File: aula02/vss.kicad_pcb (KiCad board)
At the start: 2 copper layers, 58 x 65 mm, 28 parts, among them J1 BATTERY, P1 MOTOR_L, P2 MOTOR_R, SW1 SW_SPST, U1 NUCLEO-F303K8, U2 SN754410, U3 LM78L05, U4 nRF24L01+

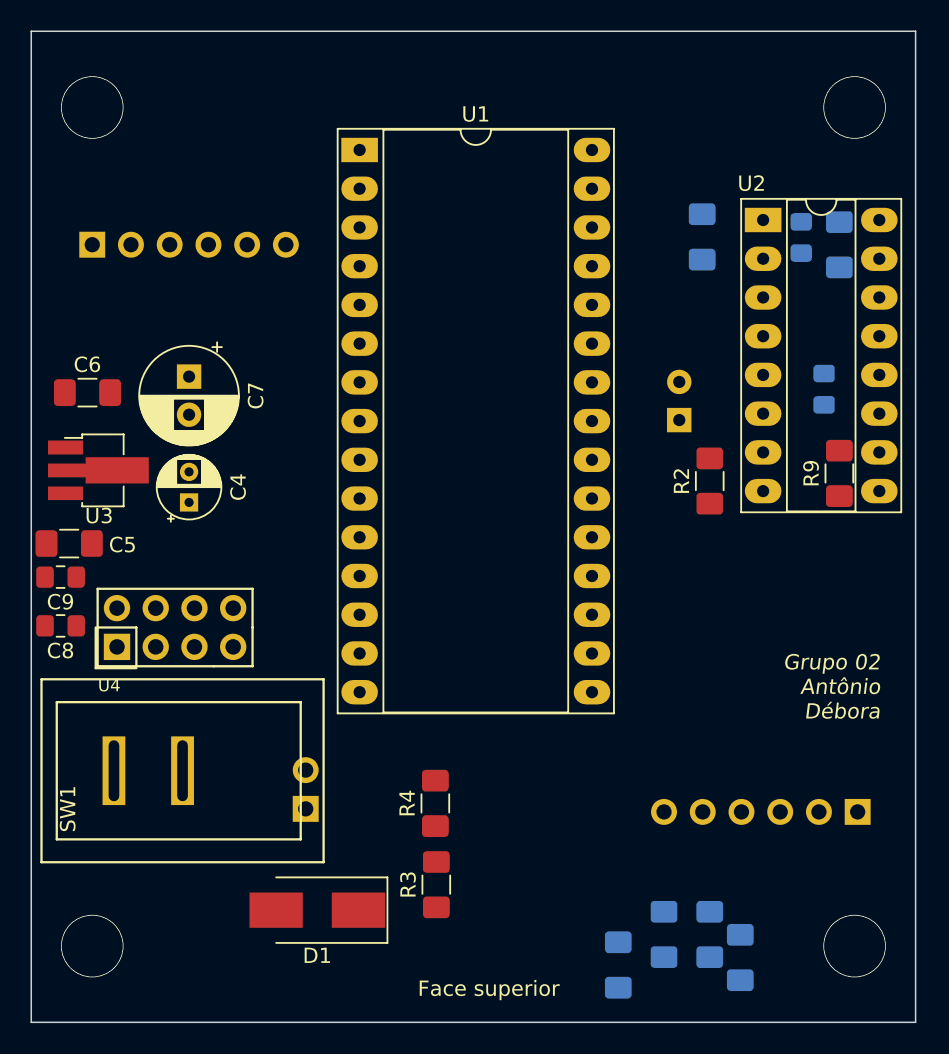
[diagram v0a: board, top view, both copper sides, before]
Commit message: feat: pcb roteamento
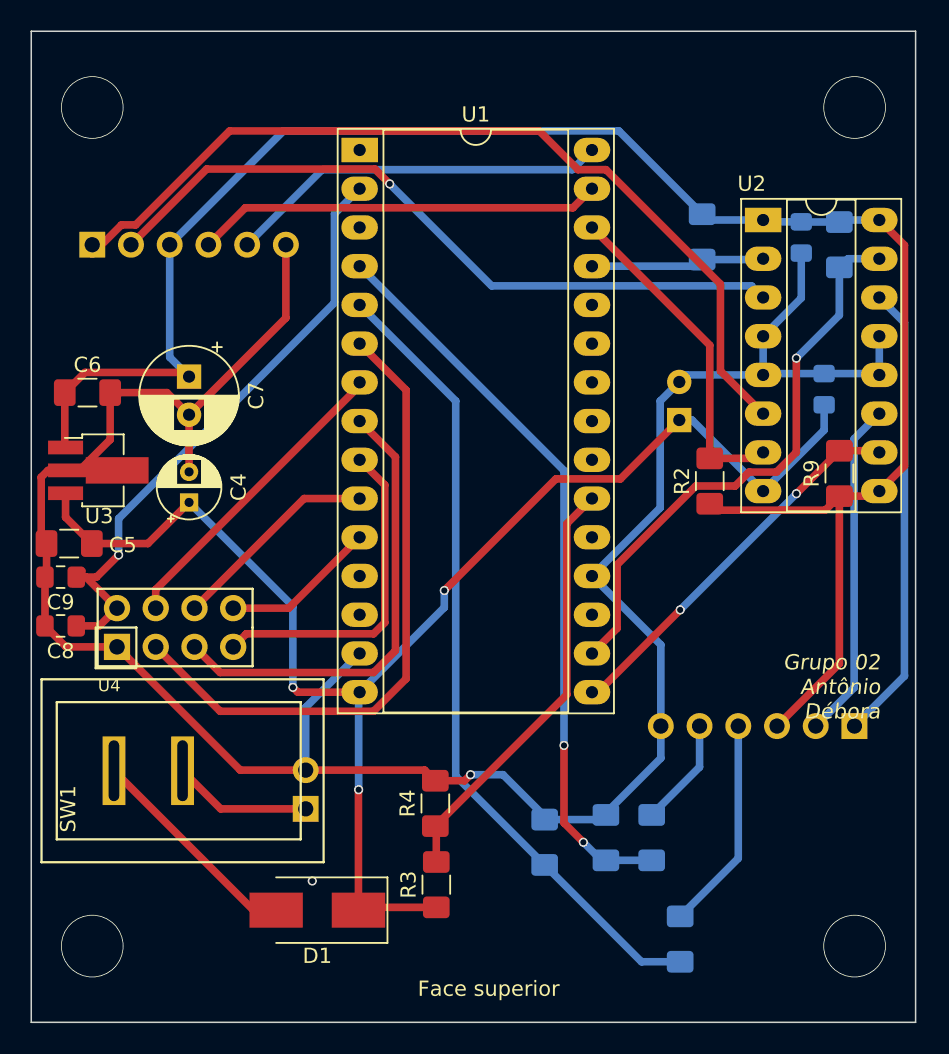
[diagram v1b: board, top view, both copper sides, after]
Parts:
- moved R7 9.39 mm to (153.7, 123.2)
- moved R6 7.41 mm to (160.7, 122.9)
- moved R8 7.41 mm to (157.7, 122.9)
- moved P2 5.63 mm to (174.0, 115.6)
- moved R5 4.12 mm to (162.6, 129.5)
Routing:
- net GND: track 0.00 -> 153.4 mm, vias 0 -> 1
- net +5V: track 0.00 -> 121.5 mm
- net +BATT: track 0.00 -> 95.4 mm, vias 0 -> 3
- net Net-(P1-Pad1): track 0.00 -> 59.0 mm
- net /MotorR/ENCODER_1: track 0.00 -> 53.3 mm
- net /MotorR/ENCODER_2: track 0.00 -> 48.8 mm, vias 0 -> 2
- net Net-(P1-Pad2): track 0.00 -> 47.0 mm, vias 0 -> 1
- net /Radio/CE: track 0.00 -> 42.3 mm
- net +3V3: track 0.00 -> 41.2 mm, vias 0 -> 1
- net /MotorR/PWM_2: track 0.00 -> 37.5 mm, vias 0 -> 1
- net /Radio/SCK: track 0.00 -> 30.5 mm
- net Net-(P2-Pad1): track 0.00 -> 30.2 mm
- net /Microcontroller/BATTERY_VOLTAGE: track 0.00 -> 28.1 mm
- net /MotorL/ENCODER_1: track 0.00 -> 26.7 mm
- net /MotorR/PWM_1: track 0.00 -> 25.8 mm, vias 0 -> 2
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
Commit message: fix: roteamento motor
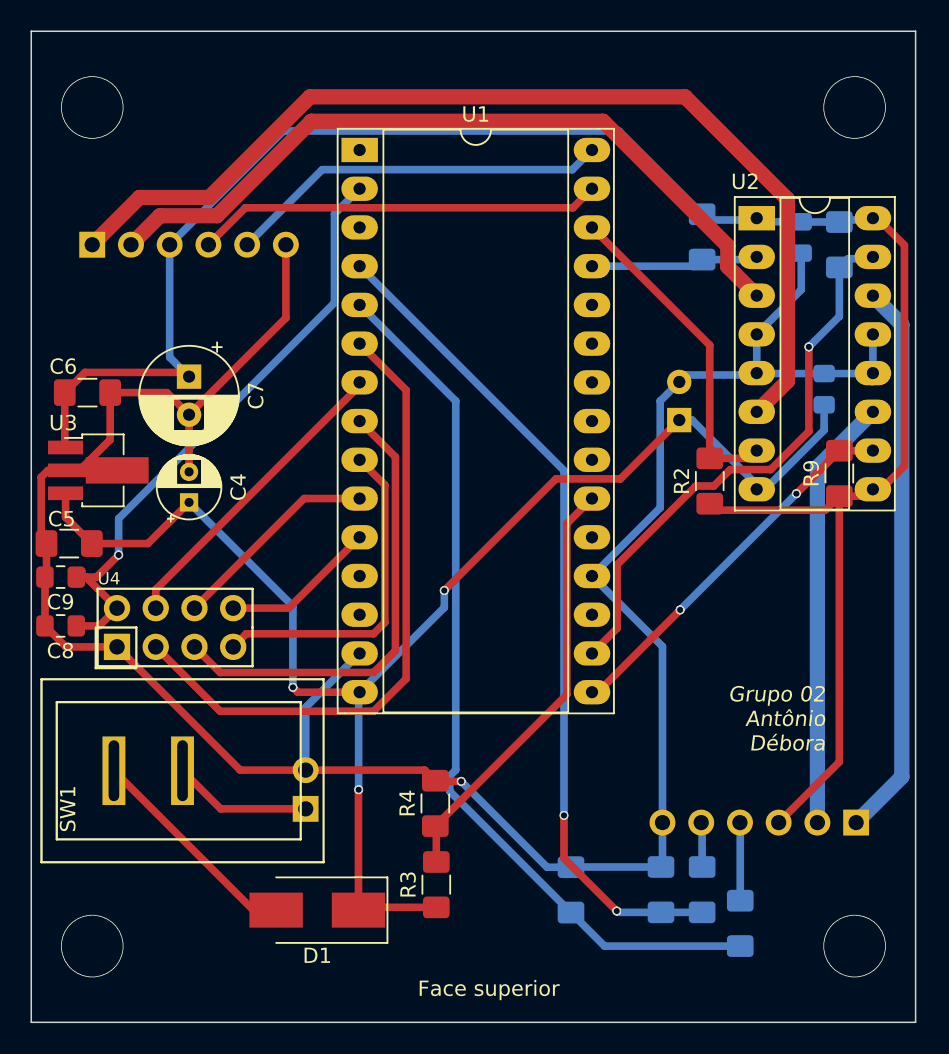
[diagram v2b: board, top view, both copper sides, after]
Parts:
- moved P2 6.33 mm to (174.1, 121.9)
- moved R8 4.97 mm to (161.3, 126.3)
- moved R6 4.75 mm to (164.0, 126.3)
- moved R5 4.07 mm to (166.5, 128.5)
- moved R7 3.57 mm to (155.4, 126.3)
- moved U2 0.44 mm to (167.6, 82.3)
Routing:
- net /MotorR/ENC_R_1: track 14.1 -> 5.13 mm
- net Net-(P1-Pad1): track 59.0 -> 67.8 mm
- net GND: track 153.4 -> 160.1 mm
- net Net-(P2-Pad1): track 30.2 -> 36.6 mm
- net +5V: track 121.5 -> 127.8 mm
- net Net-(P2-Pad2): track 22.2 -> 28.4 mm
- net /MotorR/ENCODER_2: track 48.8 -> 54.9 mm
- net /MotorR/ENCODER_1: track 53.3 -> 58.5 mm
- net /MotorR/ENC_R_2: track 7.13 -> 2.94 mm
- net Net-(P1-Pad2): track 47.0 -> 50.2 mm, vias 1 -> 0
- net (no net): vias 5 -> 4
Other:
- board text added: "GND"

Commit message: fix: roteamento motor
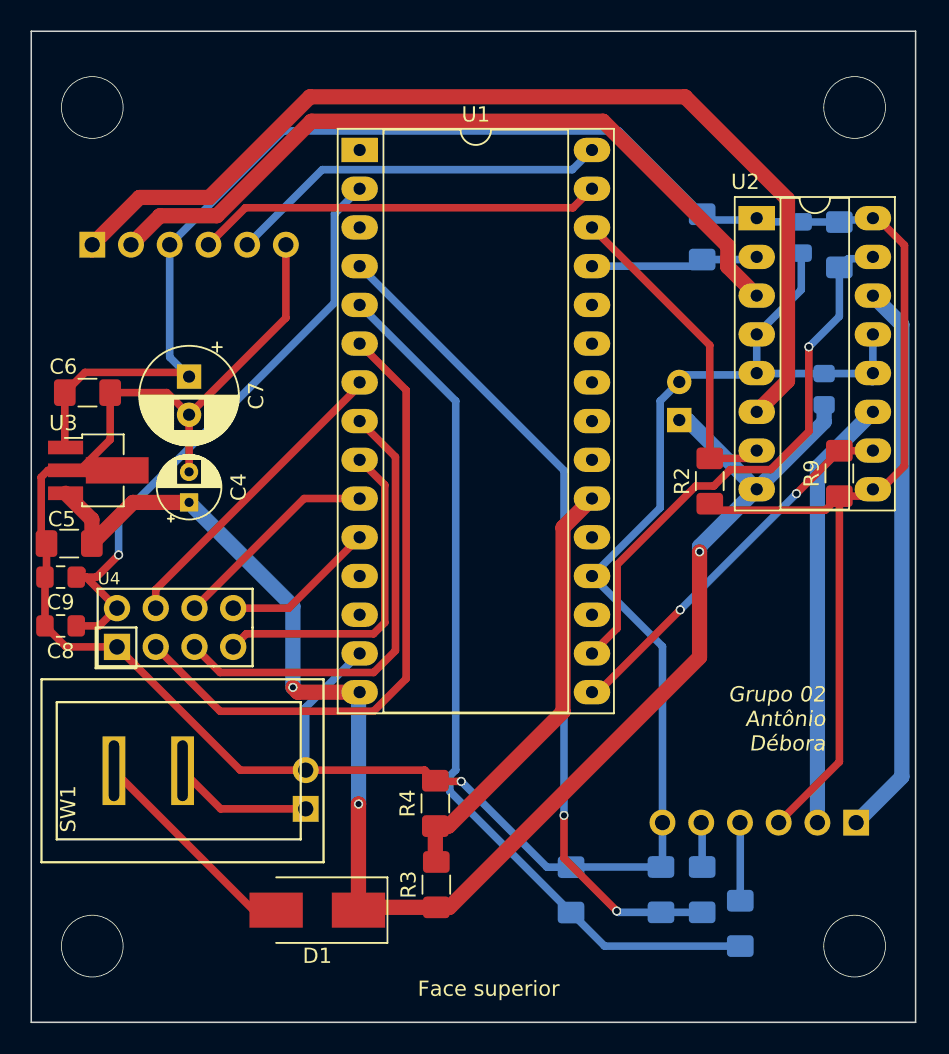
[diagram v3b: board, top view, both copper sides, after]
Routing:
- net +BATT: track 95.4 -> 102.8 mm
- net /Microcontroller/BATTERY_VOLTAGE: track 28.1 -> 28.7 mm

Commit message: fix: plano de ground
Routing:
- net GND: track 160.1 -> 29.4 mm, vias 1 -> 21
- added copper zone on B.Cu, net GND
- added copper zone on F.Cu, net GND
